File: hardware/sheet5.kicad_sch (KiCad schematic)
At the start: 2 parts

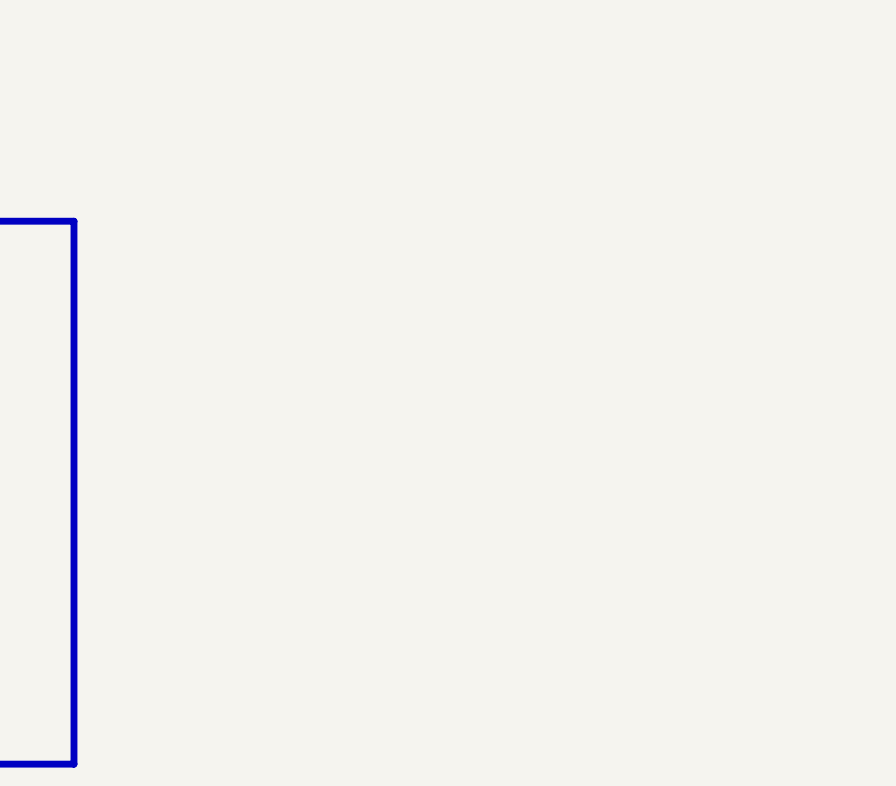
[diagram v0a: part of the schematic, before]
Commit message: hardware(feat): add spi nor flash with cs pull-up and decoupling (#6)
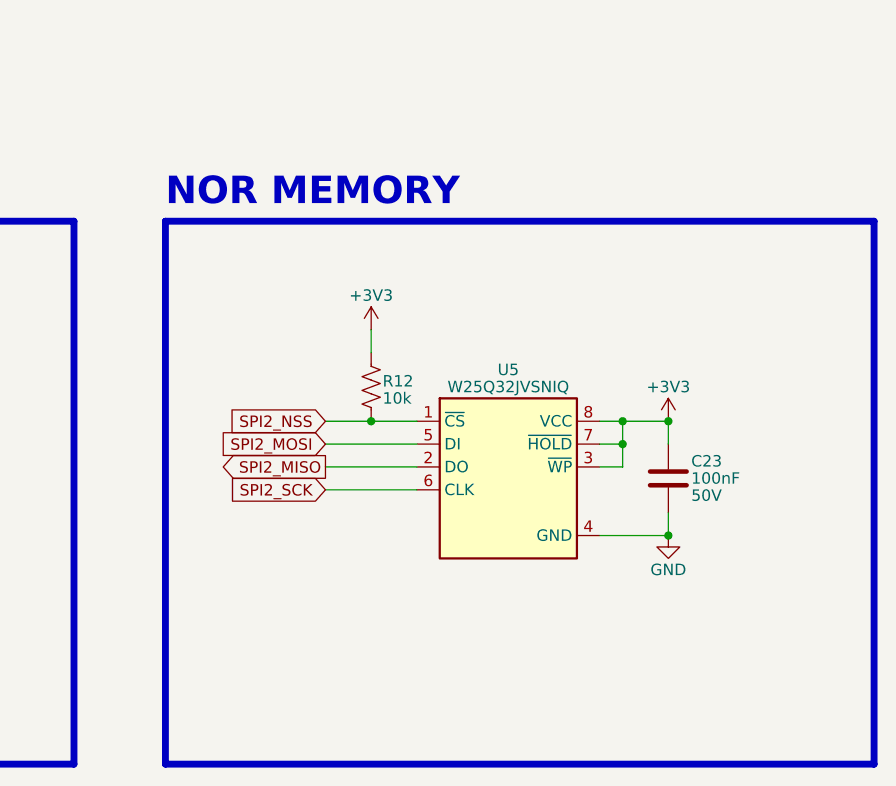
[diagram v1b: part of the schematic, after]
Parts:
- added C23: 100nF, 02_capacitors:C_0603_1608Metric, symbol 02_capacitors:CAP_100nF-50V-10%-X7R-0603
- added R12: 10k, 01_resistors:R_0603_1608Metric, symbol 01_resistors:RES_10K-0.1W-1%-0603
- added U5: W25Q32JVSNIQ, 06_ics:SOIC-8_3.9x4.9mm_P1.27mm, symbol 06_ics:IC-MEM_W25Q32JVSNIQ
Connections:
- net +3V3: now also C23.1, R12.1, U5.3 (~{WP}), U5.7 (~{HOLD}), U5.8 (VCC)
- net GND: now also C23.2, U5.4 (GND)
- new net SPI2_MISO: U5.2 (DO)
- new net SPI2_MOSI: U5.5 (DI)
- new net SPI2_NSS: R12.2, U5.1 (~{CS})
- new net SPI2_SCK: U5.6 (CLK)
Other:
- note added: "NOR MEMORY"
